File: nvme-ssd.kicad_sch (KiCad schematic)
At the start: 20 parts, among them J3 1-2199230-6

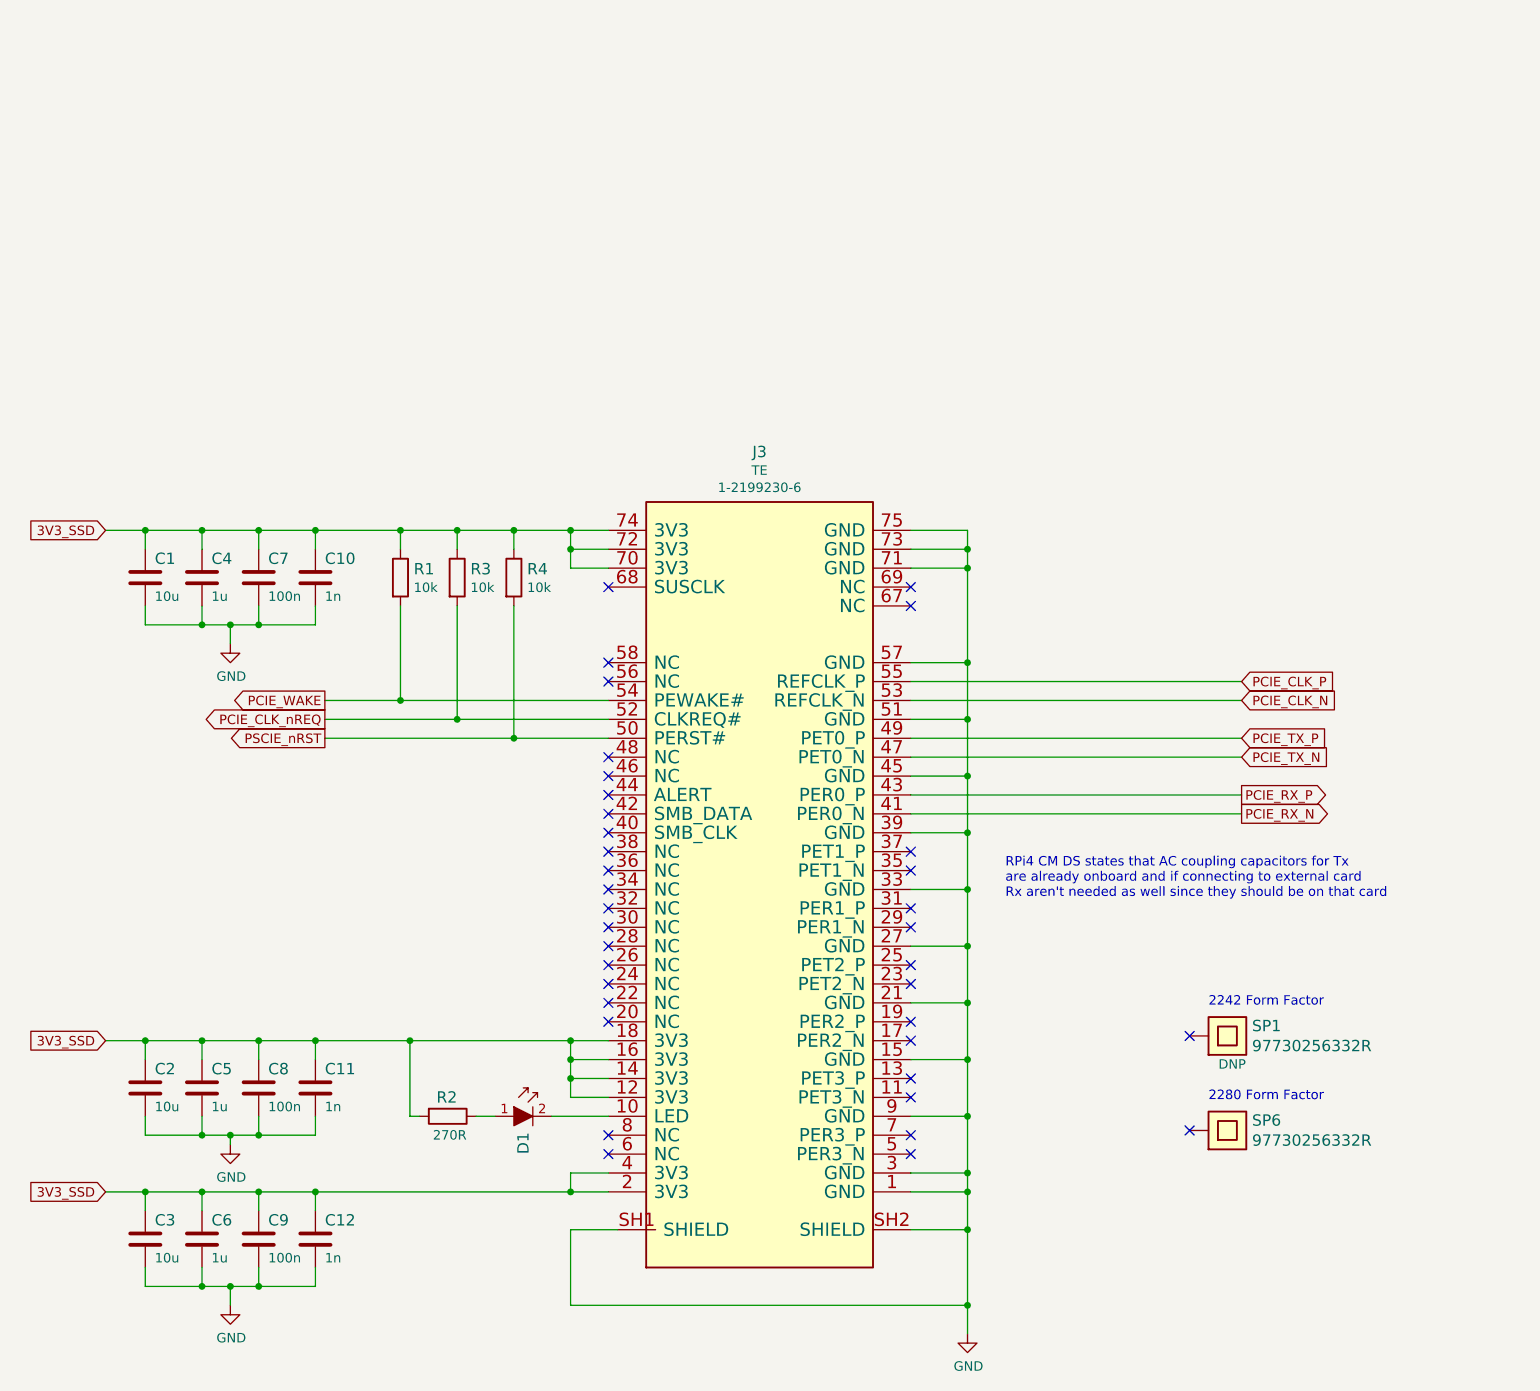
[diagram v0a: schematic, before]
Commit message: Update 1-2199230-6 symbol and footprint
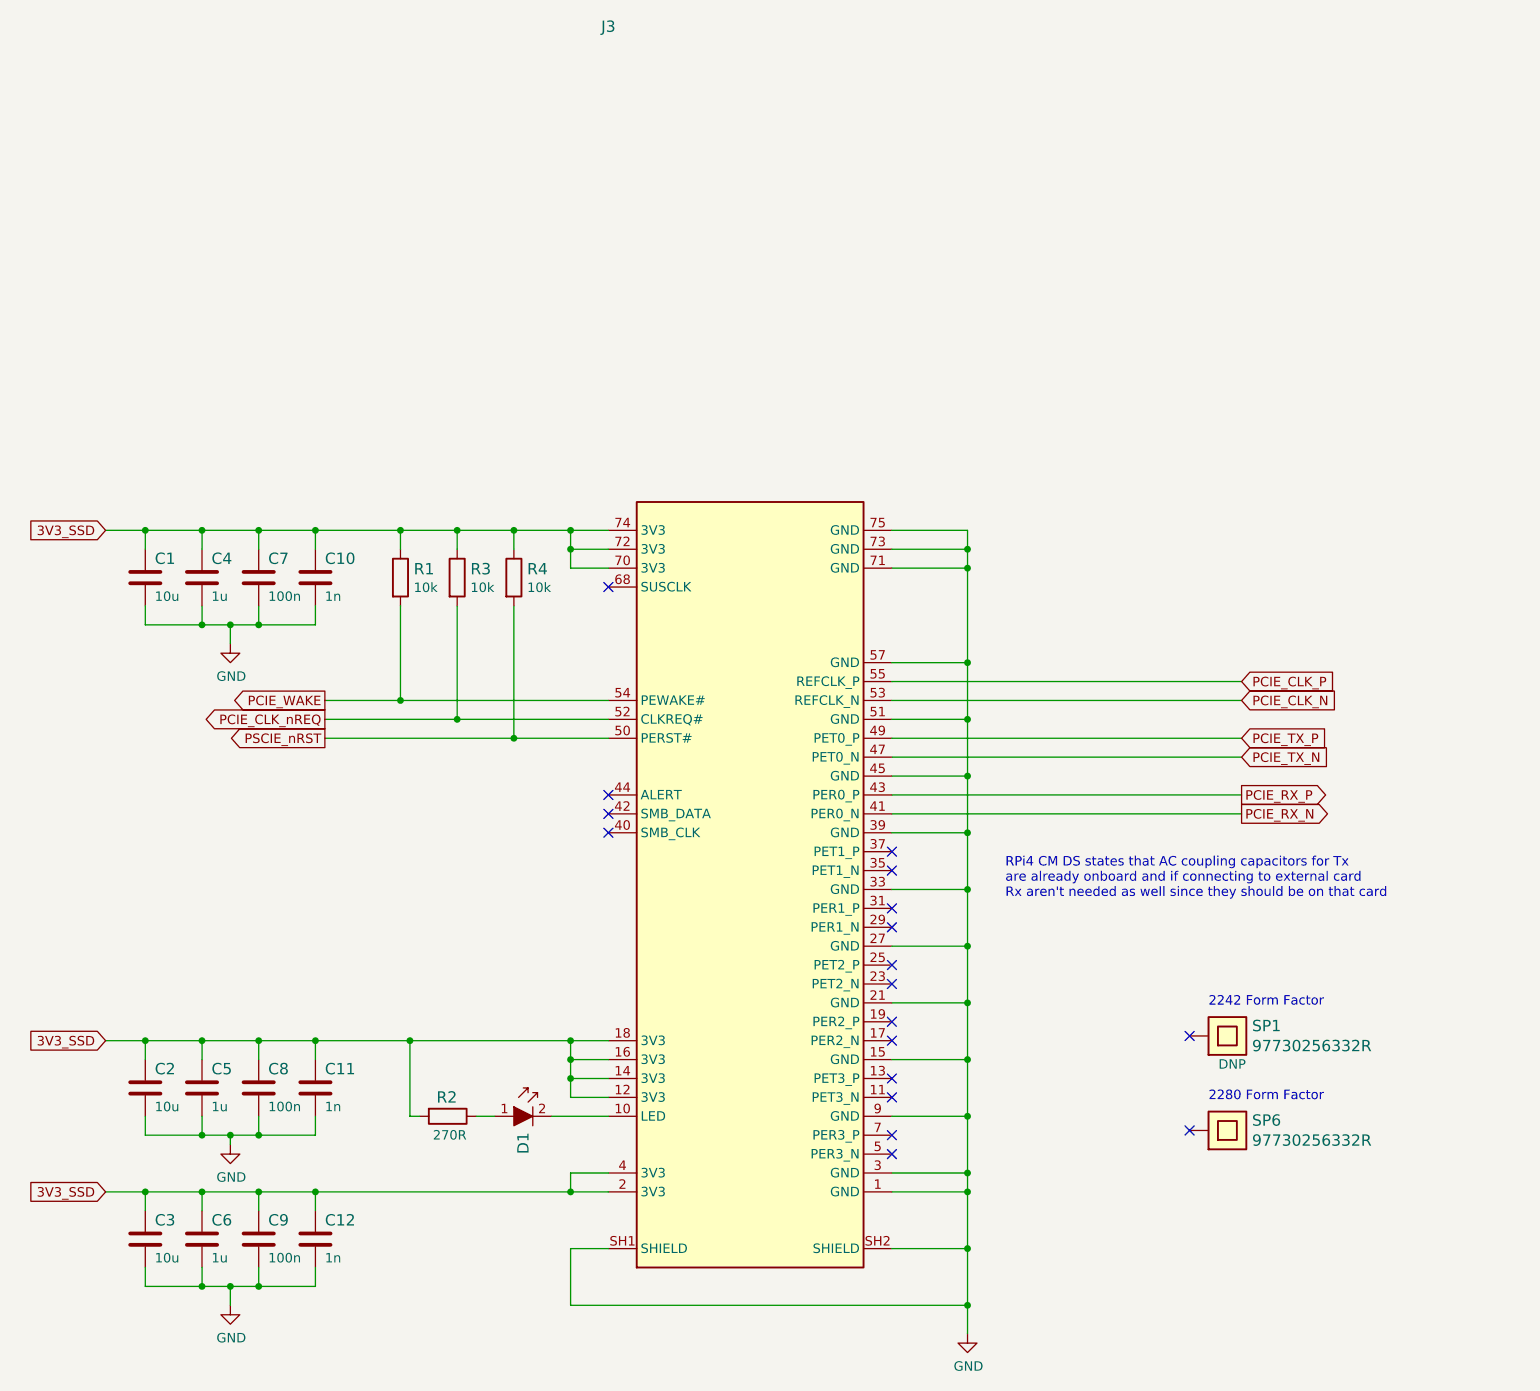
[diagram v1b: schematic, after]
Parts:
- J3: footprint scalenode-cm4-baseboard-footprints:1-2199230-6 -> antmicro-footprints:1-2199230-6; symbol scalenode-cm4-baseboard:1-2199230-6 -> antmicroPciConnectors:Bus_M.2-0.5P-1-2199230-6; Author (none) -> Antmicro; License (none) -> Apache-2.0
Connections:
- no-connect marks 36 -> 18

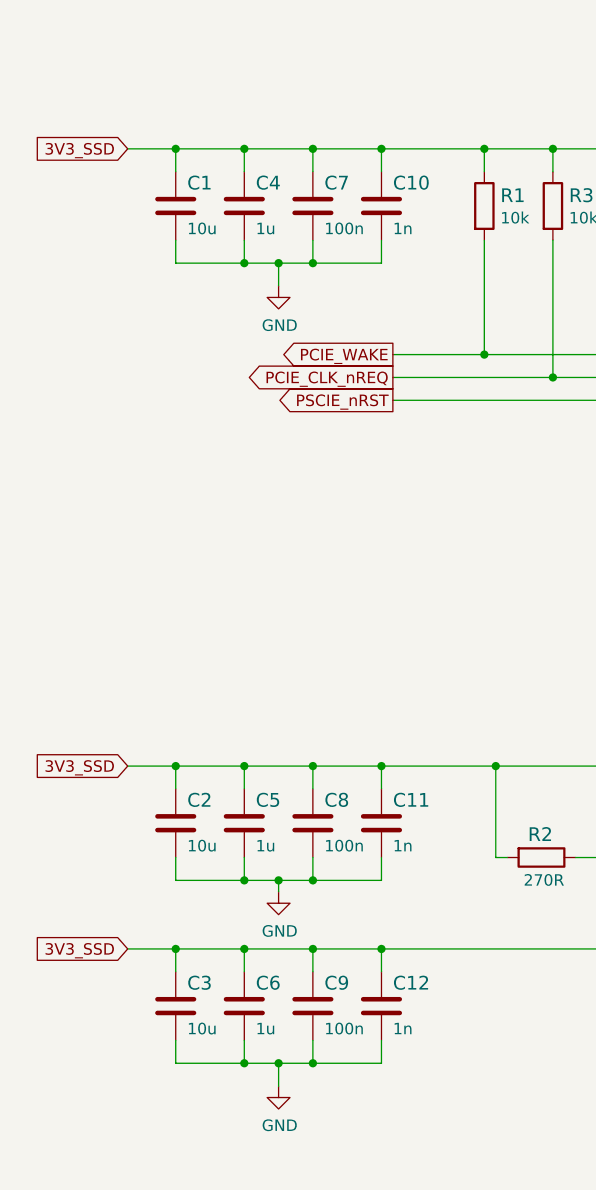
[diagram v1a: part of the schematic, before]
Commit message: Update C1,C2,C3 symbol and footprint
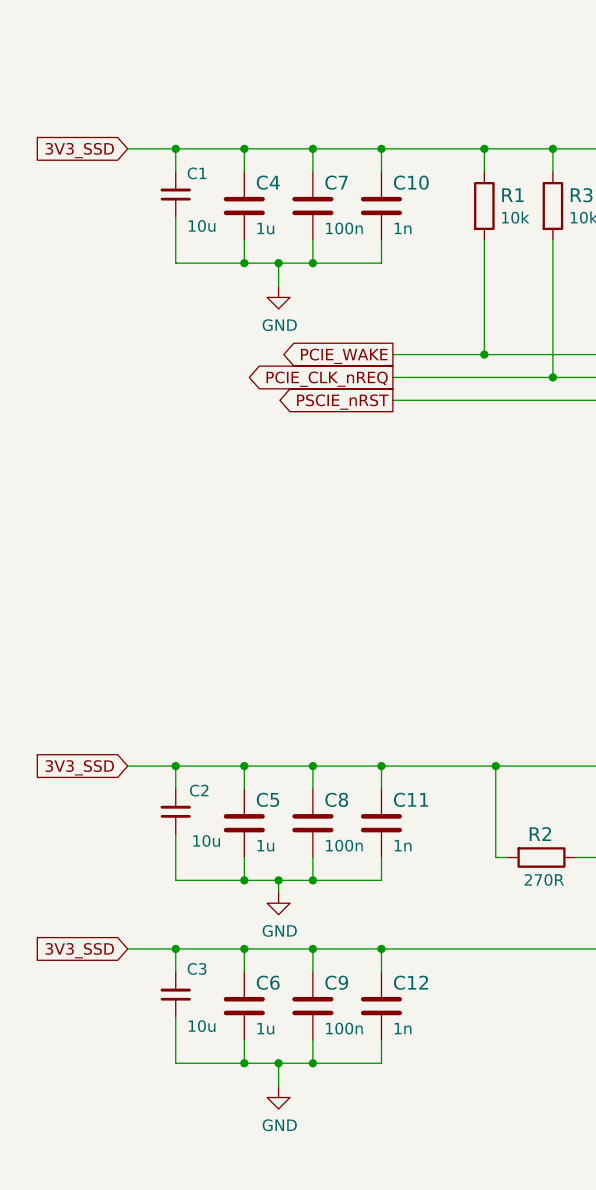
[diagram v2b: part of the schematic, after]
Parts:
- C1, C2, C3: footprint scalenode-cm4-baseboard-footprints:0603-cap -> antmicro-footprints:C_0603_1608Metric; symbol scalenode-cm4-baseboard:C_10u_0603 -> antmicroCapacitors0603:C_10u_0603; Author (none) -> Antmicro; License (none) -> Apache-2.0
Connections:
- net 3V3_SSD: now also C1.2, C2.2, C3.2; no longer C1.1, C2.1, C3.1
- net GND: now also C1.1, C2.1, C3.1; no longer C1.2, C2.2, C3.2
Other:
- moved on the sheet: C1, C2, C3
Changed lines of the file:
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@@
     (stroke (width 0) (type default) (color 0 0 0 0))
   )
-  (wire (pts (xy 71.12 54.61) (xy 71.12 57.15))
+  (wire (pts (xy 71.12 52.07) (xy 71.12 57.15))
     (stroke (width 0) (type default) (color 0 0 0 0))
   )
@@
     (stroke (width 0) (type default) (color 0 0 0 0))
   )
+  (wire (pts (xy 71.12 44.45) (xy 71.12 46.99))
+    (stroke (width 0) (type default) (color 0 0 0 0))
+  )
+  (wire (pts (xy 71.12 113.03) (xy 71.12 115.57))
+    (stroke (width 0) (type default) (color 0 0 0 0))
+  )
   (wire (pts (xy 78.74 57.15) (xy 82.55 57.15))
     (stroke (width 0) (type default) (color 0 0 0 0))
@@
     (stroke (width 0) (type default) (color 0 0 0 0))
   )
-  (wire (pts (xy 71.12 113.03) (xy 71.12 115.57))
-    (stroke (width 0) (type default) (color 0 0 0 0))
-  )
   (wire (pts (xy 133.35 133.35) (xy 128.27 133.35))
     (stroke (width 0) (type default) (color 0 0 0 0))
@@
     (stroke (width 0) (type default) (color 0 0 0 0))
   )
-  (wire (pts (xy 71.12 143.51) (xy 71.12 146.05))
-    (stroke (width 0) (type default) (color 0 0 0 0))
-  )
   (wire (pts (xy 78.74 146.05) (xy 82.55 146.05))
     (stroke (width 0) (type default) (color 0 0 0 0))
@@
     (stroke (width 0) (type default) (color 0 0 0 0))
   )
+  (wire (pts (xy 71.12 140.97) (xy 71.12 146.05))
+    (stroke (width 0) (type default) (color 0 0 0 0))
+  )
   (wire (pts (xy 71.12 133.35) (xy 65.786 133.35))
     (stroke (width 0) (type default) (color 0 0 0 0))
@@
     (stroke (width 0) (type default) (color 0 0 0 0))
   )
-  (wire (pts (xy 71.12 123.19) (xy 71.12 125.73))
+  (wire (pts (xy 71.12 120.65) (xy 71.12 125.73))
     (stroke (width 0) (type default) (color 0 0 0 0))
   )
@@
   )
   (wire (pts (xy 78.74 57.15) (xy 78.74 54.61))
-    (stroke (width 0) (type default) (color 0 0 0 0))
-  )
-  (wire (pts (xy 71.12 44.45) (xy 71.12 46.99))
     (stroke (width 0) (type default) (color 0 0 0 0))
   )
@@
     (pin "1")
   )
-  (symbol (lib_id "scalenode-cm4-baseboard:C_10u_0603") (at 71.12 119.38 0) (unit 1)
+  (symbol (lib_id "antmicroCapacitors0603:C_10u_0603") (at 71.12 120.65 90) (unit 1)
     (in_bom yes) (on_board yes)
-    (property "Reference" "C2" (id 0) (at 72.39 116.84 0)
-      (effects (font (size 1.524 1.524)) (justify left))
-    )
-    (property "Value" "C_10u_0603" (id 1) (at 71.12 123.19 0)
-      (effects (font (size 1.524 1.524)) hide)
-    )
-    (property "Footprint" "scalenode-cm4-baseboard-footprints:0603-cap" (id 2) (at 76.2 114.3 0)
-      (effects (font (size 1.524 1.524)) (justify left) hide)
-    )
-    (property "Datasheet" "" (id 3) (at 71.12 119.38 0)
-      (effects (font (size 1.27 1.27)) hide)
-    )
-    (property "Manufacturer" "Murata" (id 4) (at 76.2 109.22 0)
-      (effects (font (size 1.524 1.524)) (justify left) hide)
-    )
-    (property "MPN" "GRM188R61A106KE69D" (id 5) (at 76.2 111.76 0)
-      (effects (font (size 1.524 1.524)) (justify left) hide)
-    )
-    (property "Val" "10u" (id 6) (at 72.39 121.92 0)
-      (effects (font (size 1.27 1.27)) (justify left))
+    (property "Reference" "C2" (id 0) (at 74.93 115.062 90)
+      (effects (font (size 1.27 1.27) (thickness 0.15)) (justify left bottom))
+    )
+    (property "Value" "C_10u_0603" (id 1) (at 81.28 100.33 0)
+      (effects (font (size 1.27 1.27) (thickness 0.15)) (justify left bottom) hide)
+    )
+    (property "Footprint" "antmicro-footprints:C_0603_1608Metric" (id 2) (at 83.82 100.33 0)
+      (effects (font (size 1.27 1.27) (thickness 0.15)) (justify left bottom) hide)
+    )
+    (property "Datasheet" " " (id 3) (at 86.36 100.33 0)
+      (effects (font (size 1.27 1.27) (thickness 0.15)) (justify left bottom) hide)
+    )
+    (property "Manufacturer" "Murata" (id 4) (at 91.44 100.33 0)
+      (effects (font (size 1.27 1.27) (thickness 0.15)) (justify left bottom) hide)
+    )
+    (property "MPN" "GRM188R61A106KE69D" (id 5) (at 88.9 100.33 0)
+      (effects (font (size 1.27 1.27) (thickness 0.15)) (justify left bottom) hide)
+    )
+    (property "Val" "10u" (id 6) (at 76.2 120.65 90)
+      (effects (font (size 1.27 1.27) (thickness 0.15)) (justify left bottom))
+    )
+    (property "License" "Apache-2.0" (id 7) (at 93.98 100.33 0)
+      (effects (font (size 1.27 1.27) (thickness 0.15)) (justify left bottom) hide)
+    )
+    (property "Author" "Antmicro" (id 8) (at 96.52 100.33 0)
+      (effects (font (size 1.27 1.27) (thickness 0.15)) (justify left bottom) hide)
+    )
+    (property "Voltage" "" (id 9) (at 99.06 100.33 0)
+      (effects (font (size 1.27 1.27)) (justify left bottom) hide)
     )
     (pin "1")
@@
     (pin "2")
   )
-  (symbol (lib_id "scalenode-cm4-baseboard:C_10u_0603") (at 71.12 139.7 0) (unit 1)
+  (symbol (lib_id "antmicroCapacitors0603:C_10u_0603") (at 71.12 140.97 90) (unit 1)
     (in_bom yes) (on_board yes)
-    (property "Reference" "C3" (id 0) (at 72.39 137.16 0)
-      (effects (font (size 1.524 1.524)) (justify left))
-    )
-    (property "Value" "C_10u_0603" (id 1) (at 71.12 143.51 0)
-      (effects (font (size 1.524 1.524)) hide)
-    )
-    (property "Footprint" "scalenode-cm4-baseboard-footprints:0603-cap" (id 2) (at 76.2 134.62 0)
-      (effects (font (size 1.524 1.524)) (justify left) hide)
-    )
-    (property "Datasheet" "" (id 3) (at 71.12 139.7 0)
-      (effects (font (size 1.27 1.27)) hide)
-    )
-    (property "Manufacturer" "Murata" (id 4) (at 76.2 129.54 0)
-      (effects (font (size 1.524 1.524)) (justify left) hide)
-    )
-    (property "MPN" "GRM188R61A106KE69D" (id 5) (at 76.2 132.08 0)
-      (effects (font (size 1.524 1.524)) (justify left) hide)
-    )
-    (property "Val" "10u" (id 6) (at 72.39 142.24 0)
-      (effects (font (size 1.27 1.27)) (justify left))
+    (property "Reference" "C3" (id 0) (at 74.676 134.874 90)
+      (effects (font (size 1.27 1.27) (thickness 0.15)) (justify left bottom))
+    )
+    (property "Value" "C_10u_0603" (id 1) (at 81.28 120.65 0)
+      (effects (font (size 1.27 1.27) (thickness 0.15)) (justify left bottom) hide)
+    )
+    (property "Footprint" "antmicro-footprints:C_0603_1608Metric" (id 2) (at 83.82 120.65 0)
+      (effects (font (size 1.27 1.27) (thickness 0.15)) (justify left bottom) hide)
+    )
+    (property "Datasheet" " " (id 3) (at 86.36 120.65 0)
+      (effects (font (size 1.27 1.27) (thickness 0.15)) (justify left bottom) hide)
+    )
+    (property "Manufacturer" "Murata" (id 4) (at 91.44 120.65 0)
+      (effects (font (size 1.27 1.27) (thickness 0.15)) (justify left bottom) hide)
+    )
+    (property "MPN" "GRM188R61A106KE69D" (id 5) (at 88.9 120.65 0)
+      (effects (font (size 1.27 1.27) (thickness 0.15)) (justify left bottom) hide)
+    )
+    (property "Val" "10u" (id 6) (at 75.692 141.224 90)
+      (effects (font (size 1.27 1.27) (thickness 0.15)) (justify left bottom))
+    )
+    (property "License" "Apache-2.0" (id 7) (at 93.98 120.65 0)
+      (effects (font (size 1.27 1.27) (thickness 0.15)) (justify left bottom) hide)
+    )
+    (property "Author" "Antmicro" (id 8) (at 96.52 120.65 0)
+      (effects (font (size 1.27 1.27) (thickness 0.15)) (justify left bottom) hide)
+    )
+    (property "Voltage" "" (id 9) (at 99.06 120.65 0)
+      (effects (font (size 1.27 1.27)) (justify left bottom) hide)
     )
     (pin "1")
@@
     (pin "2")
   )
-  (symbol (lib_id "scalenode-cm4-baseboard:C_10u_0603") (at 71.12 50.8 0) (unit 1)
+  (symbol (lib_id "antmicroCapacitors0603:C_10u_0603") (at 71.12 52.07 90) (unit 1)
     (in_bom yes) (on_board yes)
-    (property "Reference" "C1" (id 0) (at 72.39 48.26 0)
-      (effects (font (size 1.524 1.524)) (justify left))
-    )
-    (property "Value" "C_10u_0603" (id 1) (at 71.12 54.61 0)
-      (effects (font (size 1.524 1.524)) hide)
-    )
-    (property "Footprint" "scalenode-cm4-baseboard-footprints:0603-cap" (id 2) (at 76.2 45.72 0)
-      (effects (font (size 1.524 1.524)) (justify left) hide)
-    )
-    (property "Datasheet" "" (id 3) (at 71.12 50.8 0)
-      (effects (font (size 1.27 1.27)) hide)
-    )
-    (property "Manufacturer" "Murata" (id 4) (at 76.2 40.64 0)
-      (effects (font (size 1.524 1.524)) (justify left) hide)
-    )
-    (property "MPN" "GRM188R61A106KE69D" (id 5) (at 76.2 43.18 0)
-      (effects (font (size 1.524 1.524)) (justify left) hide)
-    )
-    (property "Val" "10u" (id 6) (at 72.39 53.34 0)
-      (effects (font (size 1.27 1.27)) (justify left))
+    (property "Reference" "C1" (id 0) (at 74.676 46.482 90)
+      (effects (font (size 1.27 1.27) (thickness 0.15)) (justify left bottom))
+    )
+    (property "Value" "C_10u_0603" (id 1) (at 81.28 31.75 0)
+      (effects (font (size 1.27 1.27) (thickness 0.15)) (justify left bottom) hide)
+    )
+    (property "Footprint" "antmicro-footprints:C_0603_1608Metric" (id 2) (at 83.82 31.75 0)
+      (effects (font (size 1.27 1.27) (thickness 0.15)) (justify left bottom) hide)
+    )
+    (property "Datasheet" " " (id 3) (at 86.36 31.75 0)
+      (effects (font (size 1.27 1.27) (thickness 0.15)) (justify left bottom) hide)
+    )
+    (property "Manufacturer" "Murata" (id 4) (at 91.44 31.75 0)
+      (effects (font (size 1.27 1.27) (thickness 0.15)) (justify left bottom) hide)
+    )
+    (property "MPN" "GRM188R61A106KE69D" (id 5) (at 88.9 31.75 0)
+      (effects (font (size 1.27 1.27) (thickness 0.15)) (justify left bottom) hide)
+    )
+    (property "Val" "10u" (id 6) (at 75.692 52.324 90)
+      (effects (font (size 1.27 1.27) (thickness 0.15)) (justify left bottom))
+    )
+    (property "License" "Apache-2.0" (id 7) (at 93.98 31.75 0)
+      (effects (font (size 1.27 1.27) (thickness 0.15)) (justify left bottom) hide)
+    )
+    (property "Author" "Antmicro" (id 8) (at 96.52 31.75 0)
+      (effects (font (size 1.27 1.27) (thickness 0.15)) (justify left bottom) hide)
+    )
+    (property "Voltage" "" (id 9) (at 99.06 31.75 0)
+      (effects (font (size 1.27 1.27)) (justify left bottom) hide)
     )
     (pin "1")
